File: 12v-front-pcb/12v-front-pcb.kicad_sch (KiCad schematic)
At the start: 31 parts, among them J1 76825-0002, J10 76825-0002, J2 76825-0004, J3 76825-0004, J4 76825-0004, J5 76825-0002, J6 76825-0004, J7 76825-0002, J8 76825-0004, J9 76825-0004

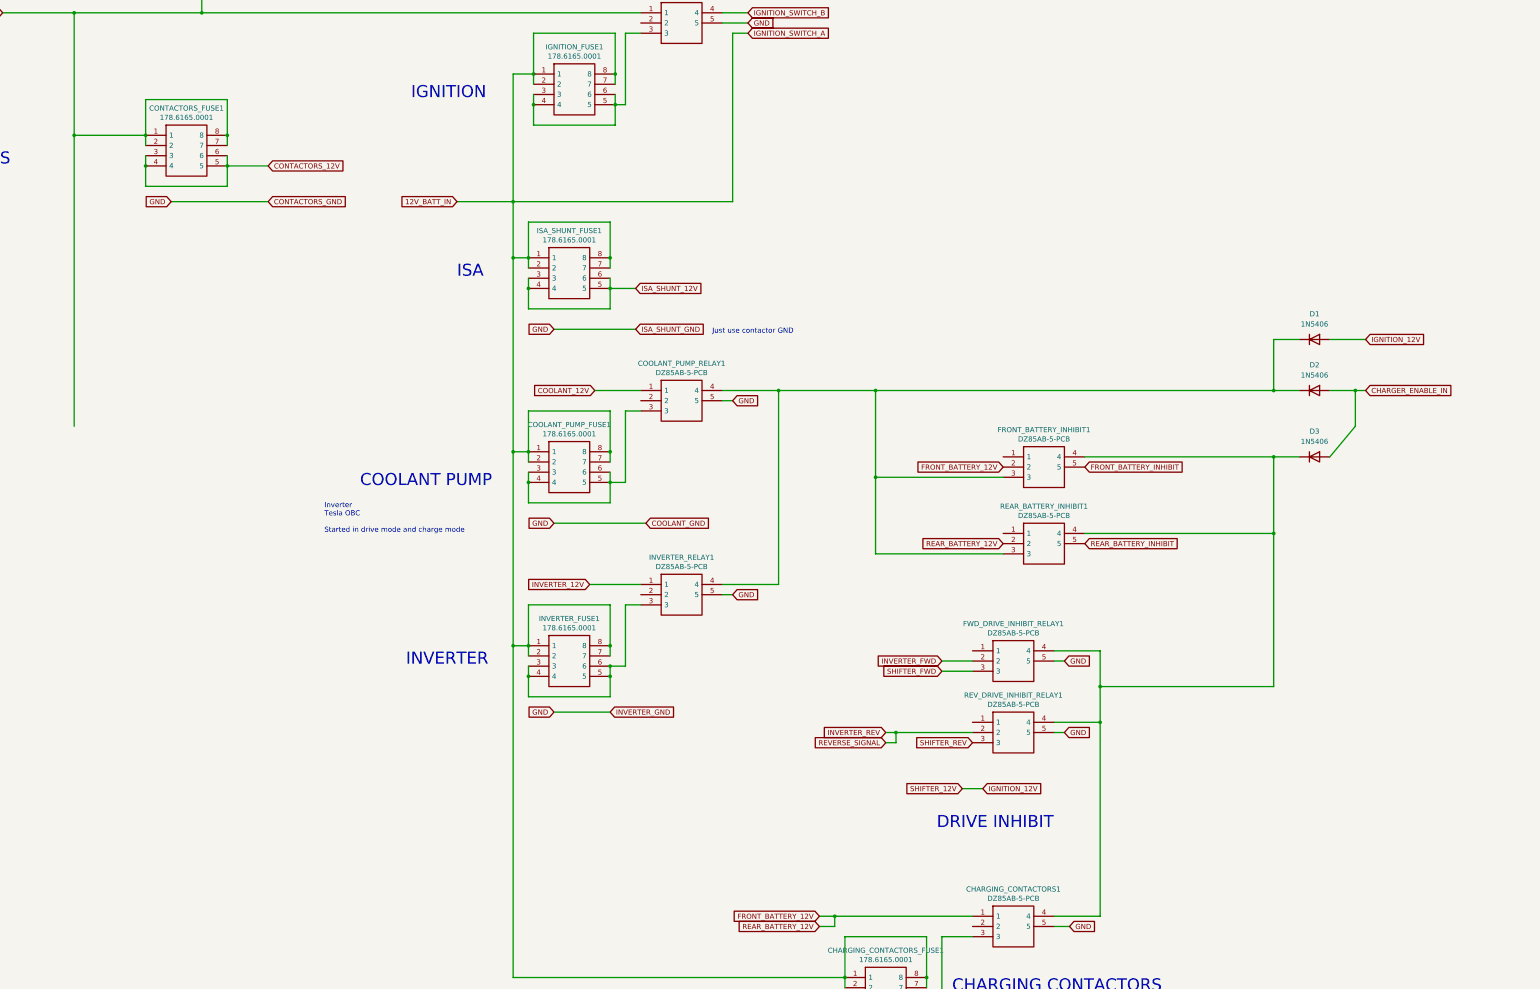
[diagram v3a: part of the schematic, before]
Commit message: 12v-front backups
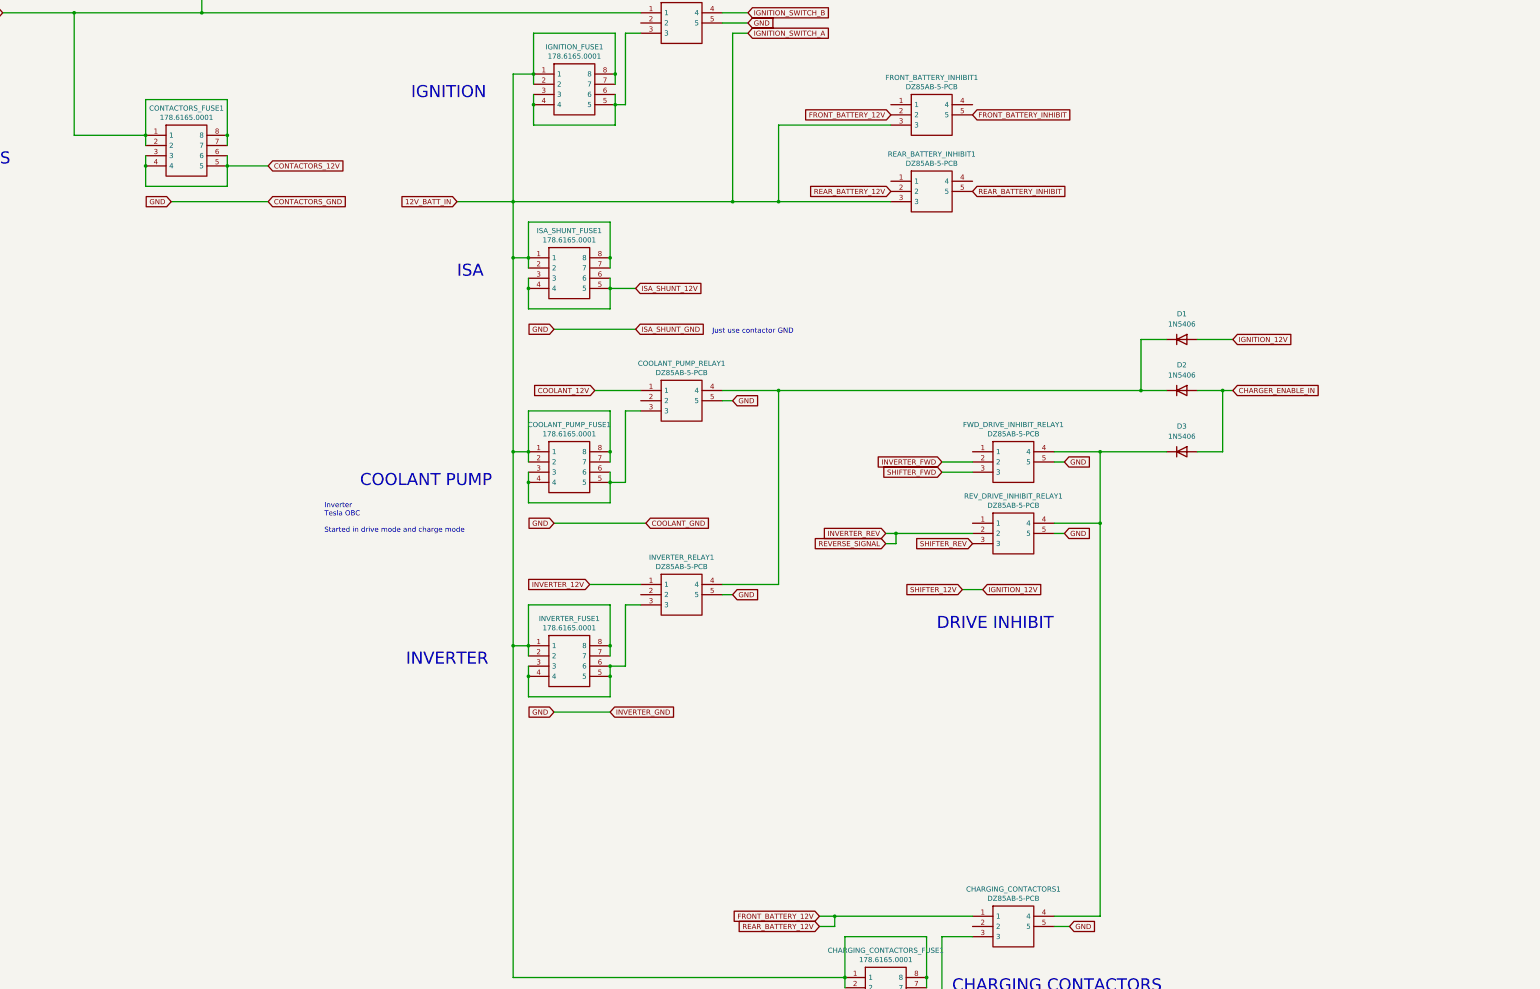
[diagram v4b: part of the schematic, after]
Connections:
- net 12V_BATT_IN: now also FRONT_BATTERY_INHIBIT1.3, REAR_BATTERY_INHIBIT1.3
- net at CHARGING_CONTACTORS1.4, D3.1 (K), FWD_DRIVE_INHIBIT_RELAY1.4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: no longer FRONT_BATTERY_INHIBIT1.4, REAR_BATTERY_INHIBIT1.4
- net at COOLANT_PUMP_RELAY1.4, D1.1 (K), D2.1 (K)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: no longer FRONT_BATTERY_INHIBIT1.3, REAR_BATTERY_INHIBIT1.3
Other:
- moved on the sheet: D1, D2, D3, FRONT_BATTERY_INHIBIT1, FWD_DRIVE_INHIBIT_RELAY1, REAR_BATTERY_INHIBIT1, REV_DRIVE_INHIBIT_RELAY1

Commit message: Errors in charge/drive mode
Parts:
- removed J5: 76825-0002, 768250002, symbol Connector:76825-0002
- removed J8, J9: 76825-0004, 768250004, symbol Connector:76825-0004
- added CRUISE_FUSE1: 178.6165.0001, Socket:17861650001, symbol Connector:178.6165.0001
- added D4: 1N5406, Diode_THT:D_DO-201AD_P15.24mm_Horizontal, symbol Diode:1N5406
- added J11, J12, J14, J15: 76825-0002, 768250002, symbol Connector:76825-0002
- added J5: 76825-0004, 768250004, symbol Connector:76825-0004
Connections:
- net INVERTER_REV is gone; now on net BRAKE_SWITCH_RETURN: J2.1, J3.3, REV_DRIVE_INHIBIT_RELAY1.2
- net 12V_BATT_IN: now also FRONT_BATTERY_INHIBIT1.4, REAR_BATTERY_INHIBIT1.4, J5.2; no longer FRONT_BATTERY_INHIBIT1.3, REAR_BATTERY_INHIBIT1.3
- net BRAKE_SWITCH_RETURN: now also J11.1
- net FRONT_BATTERY_12V: now also J15.1; no longer CHARGING_CONTACTORS1.1, REAR_BATTERY_INHIBIT1.2
- net FRONT_BATTERY_INHIBIT: now also J15.2
- net IGNITION_12V: now also J4.1, CRUISE_FUSE1.1, CRUISE_FUSE1.2, CRUISE_FUSE1.7, CRUISE_FUSE1.8; no longer J4.2
- net IGNITION_SWITCH_B: now also J5.1
- net ISA_SHUNT_12V: now also J4.2; no longer J4.1
- net REAR_BATTERY_INHIBIT: now also J14.2
- net at CHARGING_CONTACTORS1.4, D3.1 (K): now also D4.2 (A); no longer FWD_DRIVE_INHIBIT_RELAY1.4, REV_DRIVE_INHIBIT_RELAY1.4
- net at COOLANT_PUMP_RELAY1.4, D1.1 (K), D2.1 (K)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: now also FRONT_BATTERY_INHIBIT1.3, REAR_BATTERY_INHIBIT1.3
- new net CHG_CONTACTORS_12V: CHARGING_CONTACTORS1.1, J12.1
- new net CRUISE_BUTTON_RETURN: J11.2, J5.4
- new net CRUISE_BUTTON_SEND: CRUISE_FUSE1.3, CRUISE_FUSE1.4, CRUISE_FUSE1.5, CRUISE_FUSE1.6, J5.3
- new net DRIVE_INHIBIT: D4.1 (K), FWD_DRIVE_INHIBIT_RELAY1.4, REV_DRIVE_INHIBIT_RELAY1.4
- new net REAR_BATTERY_12V: J14.1, REAR_BATTERY_INHIBIT1.2
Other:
- note added: "0ma"
- note added: "160ma"
- note added: "Activated by charger only"
- note added: "Activated by ignition or charger"
- note added: "Always on"
- note added: "BRAKE SW"
- note added: "Battery box contactors"
- note added: "CONTACTORS Main Precharge"
- note added: "CRUISE"
- note added: "contactor 120ma contactor 120ma"
- note added: "pos contactor 120ma neg contactor 120ma"
- note added: "relay 160ma"
- note added: "relay 160ma relay 160ma"
- note removed: "### ToDo ### Battery tender Battery box contactors? High beam signal turn signal signal Start switch? ignition Criuse Inverter brake signal"
- note removed: "12v + gnd to negative contactor gnd to precharge and main contactors"
- note removed: "CHARGER_ON_SIGNAL - signal from rear box to indicate charging has been initiated. Turns on dashboard so it can show charge status."
- note removed: "CONTACTORS"
- note removed: "Inverter Tesla OBC Started in drive mode and charge mode"
- moved on the sheet: BRAKE_FUSE1, CHARGING_CONTACTORS1, CHARGING_CONTACTORS_FUSE1, CONTACTORS_FUSE1, COOLANT_PUMP_FUSE1, COOLANT_PUMP_RELAY1, D1, D2, D3, FRONT_BATTERY_INHIBIT1, FWD_DRIVE_INHIBIT_RELAY1, IGNITION_FUSE1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

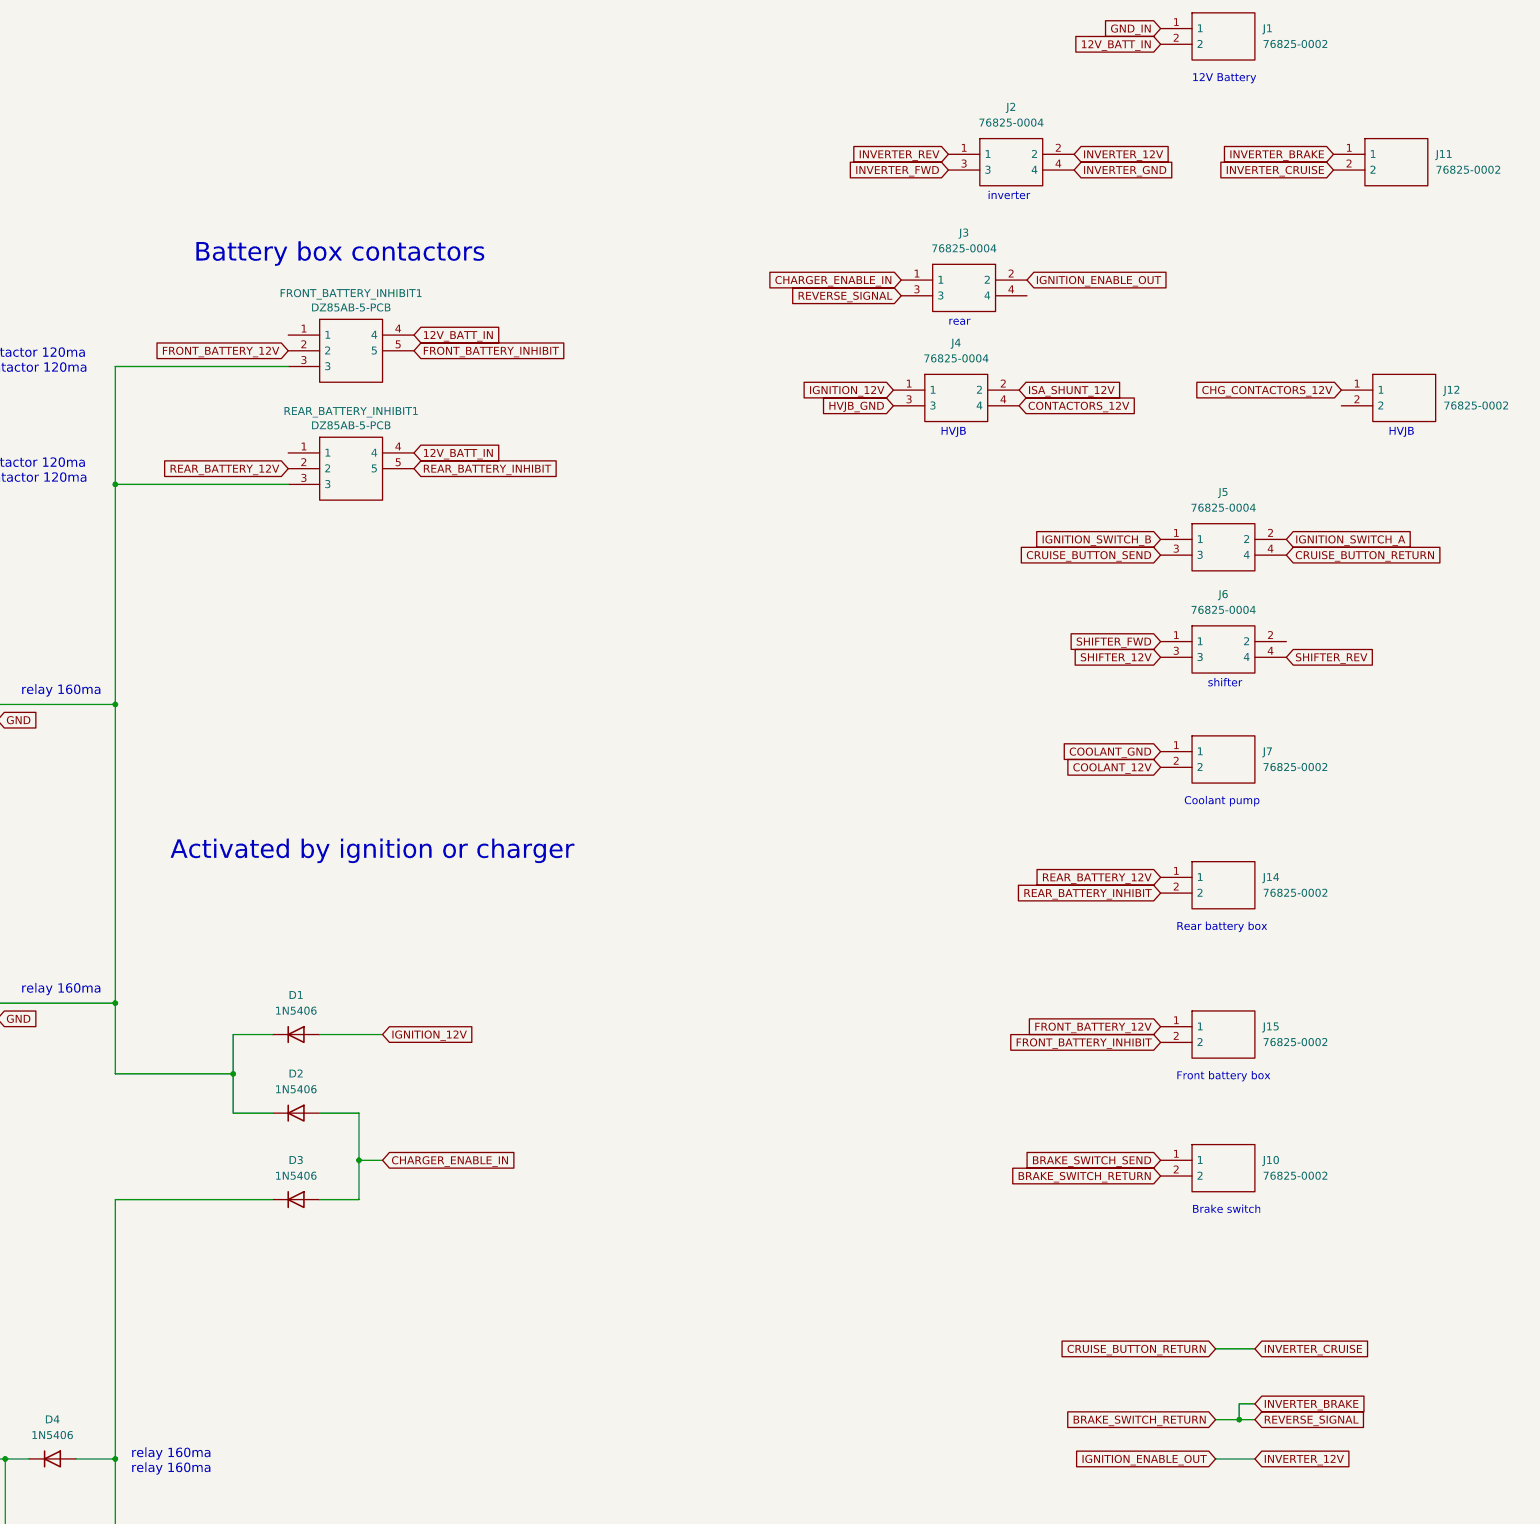
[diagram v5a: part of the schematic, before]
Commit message: Fixing issues on 12-front. lots of updates to wiring diagrams
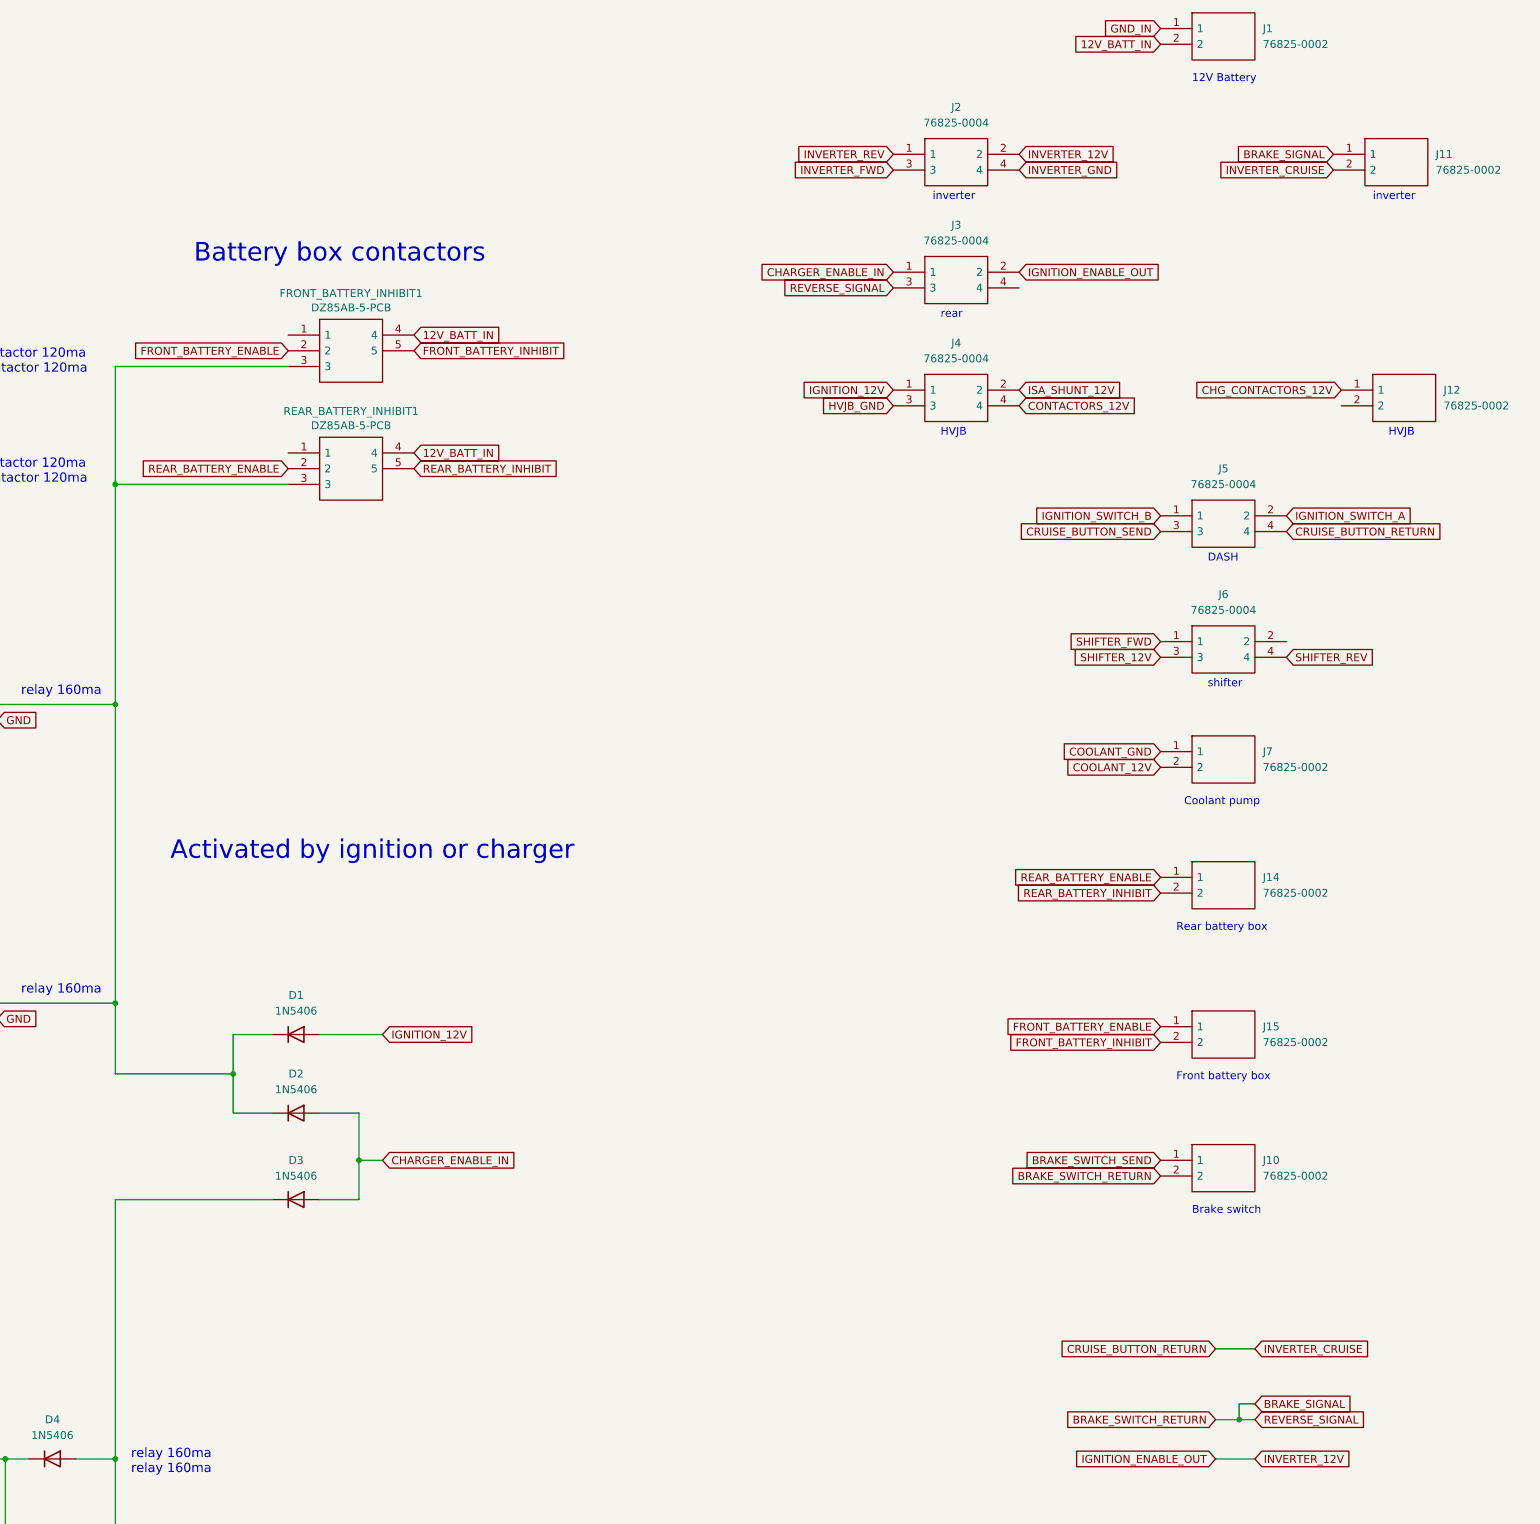
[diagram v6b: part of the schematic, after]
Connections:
- net BRAKE_SWITCH_RETURN renamed BRAKE_SIGNAL
- net FRONT_BATTERY_12V renamed FRONT_BATTERY_ENABLE
- net REAR_BATTERY_12V renamed REAR_BATTERY_ENABLE
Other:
- note added: "DASH"
- moved on the sheet: J2, J3, J5

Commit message: rework on 12v front pcb
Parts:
- removed H2, H3, H4: MountingHole, MountingHole:MountingHole_3mm, symbol Mechanical:MountingHole
- added D5, D6: LED, LED_THT:LED_D3.0mm_Clear, symbol Device:LED
- added DASH_FUSE1, WIPER_FUSE1: 178.6165.0001, Library:17861650001, symbol Connector:178.6165.0001
- added J8, J9: 76825-0004, 768250004, symbol Connector:76825-0004
- added R1, R2: R_US, Diode_THT:D_T-1_P2.54mm_Vertical_AnodeUp, symbol Device:R_US
- BRAKE_FUSE1, CHARGING_CONTACTORS_FUSE1, CONTACTORS_FUSE1, COOLANT_PUMP_FUSE1, CRUISE_FUSE1, IGNITION_FUSE1, INVERTER_FUSE1, ISA_SHUNT_FUSE1: footprint Socket:17861650001 -> Library:17861650001
- CHARGING_CONTACTORS1, COOLANT_PUMP_RELAY1, FRONT_BATTERY_INHIBIT1, FWD_DRIVE_INHIBIT_RELAY1, IGNITION_RELAY1, INVERTER_RELAY1, REAR_BATTERY_INHIBIT1, REV_DRIVE_INHIBIT_RELAY1: footprint Connector:DZ85AB5PCB -> Library:DZ85AB5PCB
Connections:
- net 12V_BATT_IN: now also DASH_FUSE1.1, DASH_FUSE1.2, DASH_FUSE1.7, DASH_FUSE1.8
- net BRAKE_SIGNAL: no longer J2.1, J3.3, REV_DRIVE_INHIBIT_RELAY1.2
- net CONTACTORS_12V: now also J4.3; no longer J4.4
- net CONTACTORS_GND: now also J7.2, D5.1 (K), D6.1 (K), J8.3; no longer J7.1
- net COOLANT_12V: now also J7.1; no longer J7.2
- net DRIVE_INHIBIT: now also J3.4
- net HVJB_GND: now also J4.4; no longer J4.3
- net IGNITION_12V: now also J8.4, J9.1, J9.2, J9.3, J9.4, R1.1, WIPER_FUSE1.1, WIPER_FUSE1.2, WIPER_FUSE1.7, WIPER_FUSE1.8
- net at CHARGING_CONTACTORS1.4, D3.1 (K), D4.2 (A): now also R2.1
- new net: D6.2 (A), R2.2
- new net: D5.2 (A), R1.2
- new net DASH_12V: DASH_FUSE1.3, DASH_FUSE1.4, DASH_FUSE1.5, DASH_FUSE1.6, J8.1
- new net INVERTER_REV: J2.1, J3.3, REV_DRIVE_INHIBIT_RELAY1.2
- new net WIPER_SWITCH_SEND: J8.2, WIPER_FUSE1.3, WIPER_FUSE1.4, WIPER_FUSE1.5, WIPER_FUSE1.6
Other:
- note added: "1000ma"
- note added: "BATTERY Direct feed from 12V Battery"
- note added: "BRAKE Brake switch"
- note added: "DASH Dash power and signals"
- note added: "DASH Ignition and cruise"
- note added: "EXTRA IGN"
- note added: "Enable signals -> 12V supply to battery box cotactors"
- note added: "FRONT BATTERY"
- note added: "HVJB Power into HVJB"
- note added: "HVJB Power to charging contactors"
- note added: "INPUTS/OUTPUTS"
- note added: "INVERTER Gear selection signals to inverter"
- note added: "INVERTER Signals"
- note added: "Inhibit signals ->low side switch from BMS"
- note added: "REAR BATTERY"
- note added: "REAR Signals to/from rear of car"
- note added: "SHIFTER Signals to/from shifter switch"
- note removed: "12V Battery"
- note removed: "Brake switch"
- note removed: "Coolant pump"
- note removed: "DASH"
- note removed: "Front battery box"
- note removed: "HVJB"
- note removed: "Rear battery box"
- note removed: "inverter"
- note removed: "rear"
- note removed: "shifter"
- moved on the sheet: CHARGING_CONTACTORS1, CHARGING_CONTACTORS_FUSE1, COOLANT_PUMP_FUSE1, COOLANT_PUMP_RELAY1, D1, D2, D3, D4, FRONT_BATTERY_INHIBIT1, FWD_DRIVE_INHIBIT_RELAY1, IGNITION_FUSE1, IGNITION_RELAY1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
